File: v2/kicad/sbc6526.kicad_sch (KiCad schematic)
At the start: 0 parts

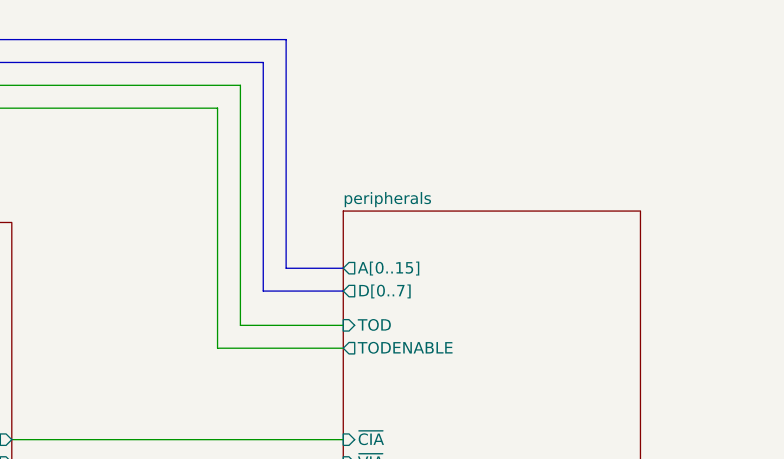
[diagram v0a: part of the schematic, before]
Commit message: PCB Tweaks
Tracks optimized.
SMD components moved to top layer.
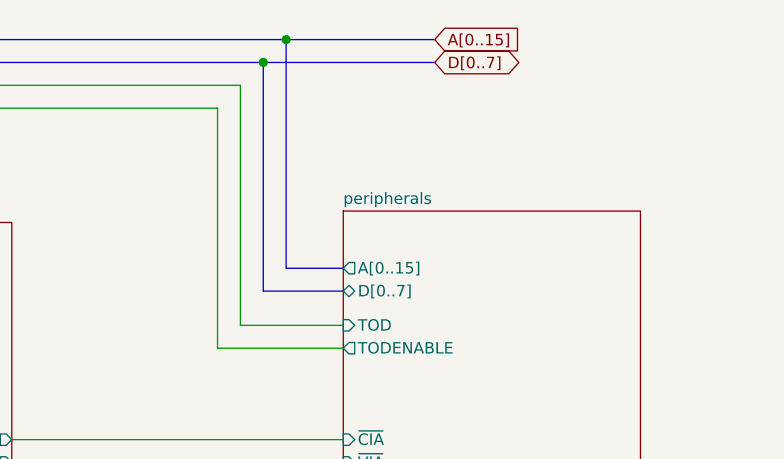
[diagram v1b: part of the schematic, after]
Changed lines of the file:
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@@
   (junction (at 153.67 27.94) (diameter 1.016) (color 0 0 0 0))
   (junction (at 156.21 25.4) (diameter 1.016) (color 0 0 0 0))
+  (junction (at 223.52 27.94) (diameter 1.016) (color 0 0 0 0))
+  (junction (at 226.06 25.4) (diameter 1.016) (color 0 0 0 0))
   (wire (pts (xy 62.23 49.53) (xy 66.04 49.53))
     (stroke (width 0) (type solid) (color 0 0 0 0))
@@
     (stroke (width 0) (type solid) (color 0 0 0 0))
   )
+  (bus (pts (xy 223.52 27.94) (xy 242.57 27.94))
+    (stroke (width 0) (type solid) (color 0 0 0 0))
+  )
   (bus (pts (xy 223.52 53.34) (xy 232.41 53.34))
     (stroke (width 0) (type solid) (color 0 0 0 0))
@@
   )
   (bus (pts (xy 226.06 25.4) (xy 226.06 50.8))
+    (stroke (width 0) (type solid) (color 0 0 0 0))
+  )
+  (bus (pts (xy 226.06 25.4) (xy 242.57 25.4))
     (stroke (width 0) (type solid) (color 0 0 0 0))
   )
@@
   (label "R~W" (at 134.62 95.25 0)
     (effects (font (size 1.27 1.27)) (justify left bottom))
+  )
+  (global_label "A[0..15]" (shape input) (at 242.57 25.4 0)    (property "Intersheet References" "${INTERSHEET_REFS}" (id 0) (at 254.1271 25.3206 0)
+      (effects (font (size 1.27 1.27)) (justify left) hide)
+    )
+    (effects (font (size 1.27 1.27)) (justify left))
+  )
+  (global_label "D[0..7]" (shape bidirectional) (at 242.57 27.94 0)    (property "Intersheet References" "${INTERSHEET_REFS}" (id 0) (at 253.099 27.8606 0)
+      (effects (font (size 1.27 1.27)) (justify left) hide)
+    )
+    (effects (font (size 1.27 1.27)) (justify left))
   )
   (sheet (at 29.21 45.72) (size 33.02 39.37)
@@
       (effects (font (size 1.27 1.27)) (justify left))
     )
-    (pin "D[0..7]" output (at 232.41 53.34 180)
-      (effects (font (size 1.27 1.27)) (justify left))
-    )
     (pin "PB[0..7]" bidirectional (at 265.43 88.9 0)
       (effects (font (size 1.27 1.27)) (justify right))
@@
     )
     (pin "~CIAEXT" input (at 232.41 74.93 180)
+      (effects (font (size 1.27 1.27)) (justify left))
+    )
+    (pin "D[0..7]" bidirectional (at 232.41 53.34 180)
       (effects (font (size 1.27 1.27)) (justify left))
     )
@@
       (reference "U8") (unit 2) (value "74AC14") (footprint "Package_SO:SOIC-14_3.9x8.7mm_P1.27mm")
     )
-    (path "/00000000-0000-0000-0000-00005fa75ce1/00000000-0000-0000-0000-00005fb33a3e"
-      (reference "#PWR0116") (unit 1) (value "GND") (footprint "")
-    )
     (path "/00000000-0000-0000-0000-00005fa75ce1/00000000-0000-0000-0000-00005fb341f3"
       (reference "#PWR0117") (unit 1) (value "GND") (footprint "")
@@
     )
     (path "/00000000-0000-0000-0000-00005fb72ec4/00000000-0000-0000-0000-00005ff8340c"
-      (reference "J1") (unit 1) (value "Conn_01x10_Female") (footprint "Connector_PinSocket_2.54mm:PinSocket_2x05_P2.54mm_Vertical")
+      (reference "PORTB1") (unit 1) (value "Conn_01x10_Female") (footprint "Connector_PinSocket_2.54mm:PinSocket_2x05_P2.54mm_Vertical")
     )
     (path "/00000000-0000-0000-0000-00005fb72ec4/00000000-0000-0000-0000-00005ff9158a"
